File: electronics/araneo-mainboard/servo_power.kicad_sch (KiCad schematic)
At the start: 1 part

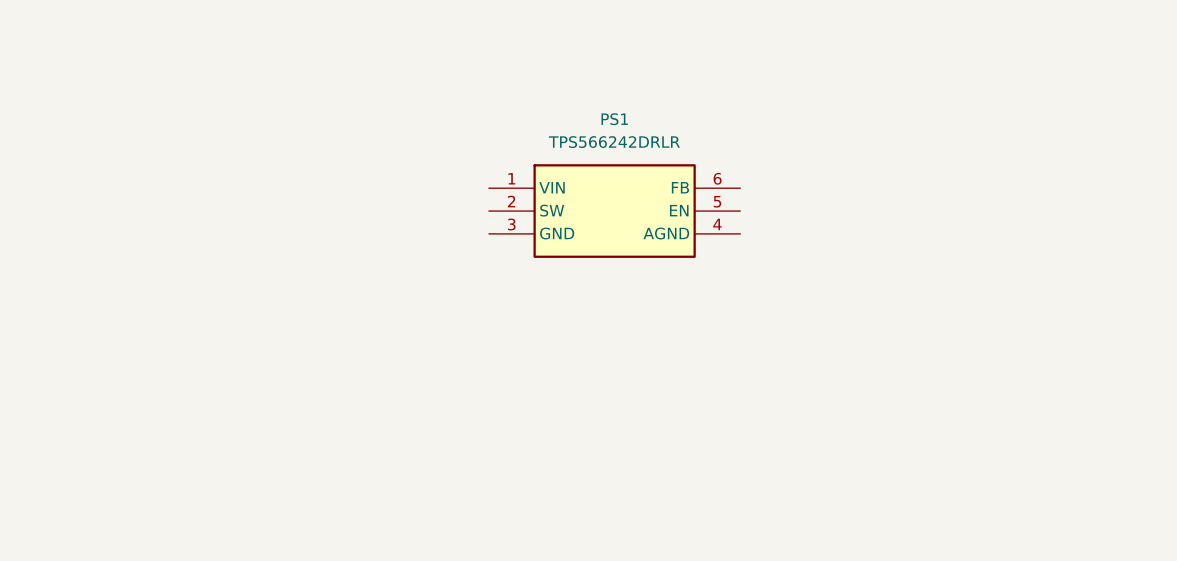
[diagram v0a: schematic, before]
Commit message: add components schematics
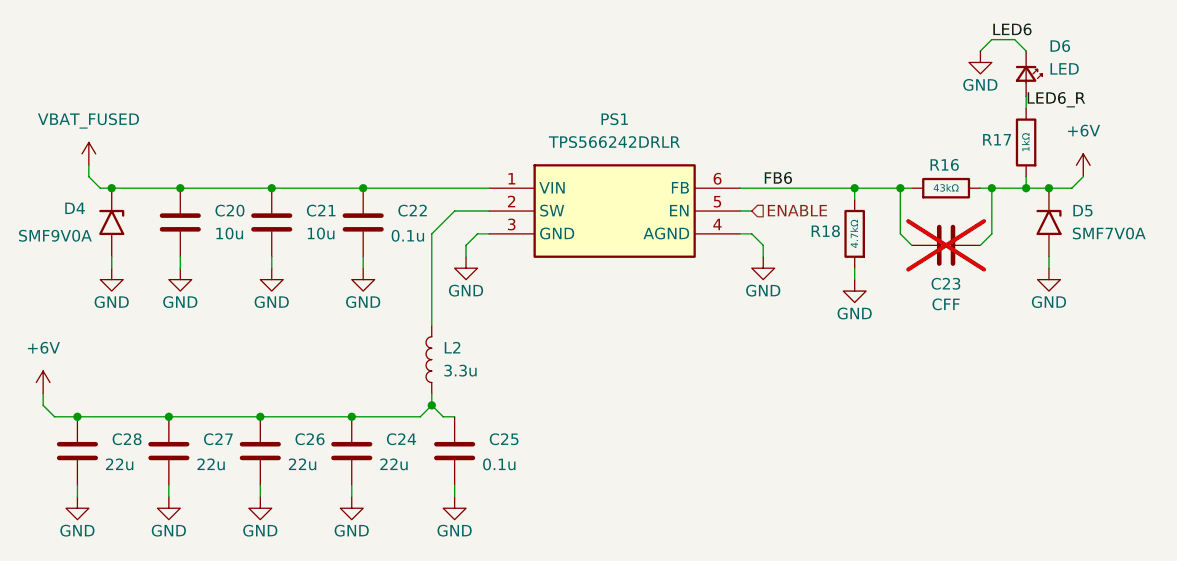
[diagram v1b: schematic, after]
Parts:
- added C20, C21: 10u, Diode_SMD:D_SMF, symbol Device:C
- added C22, C25: 0.1u, Diode_SMD:D_SMF, symbol Device:C
- added C23: CFF, Diode_SMD:D_SMF, symbol Device:C
- added C24, C26, C27, C28: 22u, Diode_SMD:D_SMF, symbol Device:C
- added D4: SMF9V0A, Diode_SMD:D_SMF, symbol Diode:SMF9V0A
- added D5: SMF7V0A, Diode_SMD:D_SMF, symbol Diode:SMF7V0A
- added D6: LED, PCM_SparkFun-LED:LED_0603_1608Metric, symbol PCM_SparkFun-LED:LED
- added L2: 3.3u, PCM_SparkFun-LED:LED_0603_1608Metric, symbol Device:L
- added R16: 43kΩ, PCM_JLCPCB:R_0402, symbol PCM_JLCPCB-Resistors:0402,1.2kΩ
- added R17: 1kΩ, PCM_JLCPCB:R_0402, symbol PCM_JLCPCB-Resistors:0402,1.2kΩ
- added R18: 4.7kΩ, PCM_JLCPCB:R_0402, symbol PCM_JLCPCB-Resistors:0402,1.2kΩ
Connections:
- net VBAT_FUSED: now reaches PS1.1 (VIN)
- net VBAT_FUSED: now also C20.1, C21.1, C22.1, D4.1 (A1)
- net at PS1.2 (SW): now also L2.2
- net GND: now reaches PS1.3 (GND)
- net GND: now also PS1.4 (AGND), C20.2, C21.2, C22.2, C24.2, C25.2, C26.2, C27.2, C28.2, D4.2 (A2), D5.2 (A2), D6.1 (K), R18.1
- net ENABLE: now reaches PS1.5 (EN)
- net FB6: now reaches PS1.6 (FB)
- net FB6: now also C23.1, R16.1, R18.2
- new net +6V: C23.2, C24.1, C25.1, C26.1, C27.1, C28.1, D5.1 (A1), L2.1, R16.2, R17.1
- new net LED6_R: D6.2 (A), R17.2

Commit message: electronics: assign footprints
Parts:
- C20, C21, C23: footprint Diode_SMD:D_SMF -> PCM_JLCPCB:C_0603
- C22, C25: footprint Diode_SMD:D_SMF -> PCM_JLCPCB:C_0402
- C24, C26, C27, C28: footprint Diode_SMD:D_SMF -> PCM_JLCPCB:C_0805
- D5: footprint Diode_SMD:D_SMF -> Diode_SMD:D_SOD-123
- D6: footprint PCM_SparkFun-LED:LED_0603_1608Metric -> PCM_JLCPCB:D_0603
- L2: footprint PCM_SparkFun-LED:LED_0603_1608Metric -> Custom:INDPM112100X400N
- PS1: footprint SOT50P160X60-6N -> Custom:SOT50P160X60-6N
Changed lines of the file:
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@@
 			)
 		)
-		(property "Footprint" "Diode_SMD:D_SMF"
+		(property "Footprint" "PCM_JLCPCB:C_0402"
 			(at 103.8352 69.85 0)
 			(hide yes)
@@
 			)
 		)
-		(property "Footprint" "Diode_SMD:D_SMF"
+		(property "Footprint" "PCM_JLCPCB:C_0805"
 			(at 72.0852 95.25 0)
 			(hide yes)
@@
 			)
 		)
-		(property "Footprint" "Diode_SMD:D_SMF"
+		(property "Footprint" "PCM_JLCPCB:C_0603"
 			(at 171.45 67.6148 0)
 			(hide yes)
@@
 			)
 		)
-		(property "Footprint" "Diode_SMD:D_SMF"
+		(property "Footprint" "PCM_JLCPCB:C_0402"
 			(at 113.9952 95.25 0)
 			(hide yes)
@@
 			)
 		)
-		(property "Footprint" "Diode_SMD:D_SMF"
+		(property "Footprint" "PCM_JLCPCB:C_0805"
 			(at 102.5652 95.25 0)
 			(hide yes)
@@
 			)
 		)
-		(property "Footprint" "PCM_SparkFun-LED:LED_0603_1608Metric"
+		(property "Footprint" "Custom:INDPM112100X400N"
 			(at 110.49 81.28 0)
 			(hide yes)
@@
 			)
 		)
-		(property "Footprint" "Diode_SMD:D_SMF"
+		(property "Footprint" "PCM_JLCPCB:C_0603"
 			(at 93.6752 69.85 0)
 			(hide yes)
@@
 			)
 		)
-		(property "Footprint" "Diode_SMD:D_SMF"
+		(property "Footprint" "PCM_JLCPCB:C_0805"
 			(at 82.2452 95.25 0)
 			(hide yes)
@@
 			)
 		)
-		(property "Footprint" "SOT50P160X60-6N"
+		(property "Footprint" "Custom:SOT50P160X60-6N"
 			(at 140.97 157.15 0)
 			(hide yes)
@@
 			)
 		)
-		(property "Footprint" "Diode_SMD:D_SMF"
+		(property "Footprint" "Diode_SMD:D_SOD-123"
 			(at 173.99 66.04 0)
 			(hide yes)
@@
 			)
 		)
-		(property "Footprint" "PCM_SparkFun-LED:LED_0603_1608Metric"
+		(property "Footprint" "PCM_JLCPCB:D_0603"
 			(at 171.45 49.53 0)
 			(hide yes)
@@
 			)
 		)
-		(property "Footprint" "Diode_SMD:D_SMF"
+		(property "Footprint" "PCM_JLCPCB:C_0805"
 			(at 92.4052 95.25 0)
 			(hide yes)
@@
 			)
 		)
-		(property "Footprint" "Diode_SMD:D_SMF"
+		(property "Footprint" "PCM_JLCPCB:C_0603"
 			(at 83.5152 69.85 0)
 			(hide yes)

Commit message: add first layout
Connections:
- net SW: now reaches L2.2, PS1.2 (SW)
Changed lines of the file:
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@@
+		)
+	)
+	(label "SW"
+		(at 110.49 74.93 90)
+		(effects
+			(font
+				(size 1.27 1.27)
+			)
+			(justify left bottom)
 		)
 	)

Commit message: electronics: update bom
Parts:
- D6, L2: now left out of the parts list
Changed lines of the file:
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@@
 		(body_style 1)
 		(exclude_from_sim no)
-		(in_bom yes)
+		(in_bom no)
 		(on_board yes)
 		(in_pos_files yes)
@@
 		(body_style 1)
 		(exclude_from_sim no)
-		(in_bom yes)
-		(on_board yes)
-		(in_pos_files yes)
+		(in_bom no)
+		(on_board yes)
+		(in_pos_files yes)

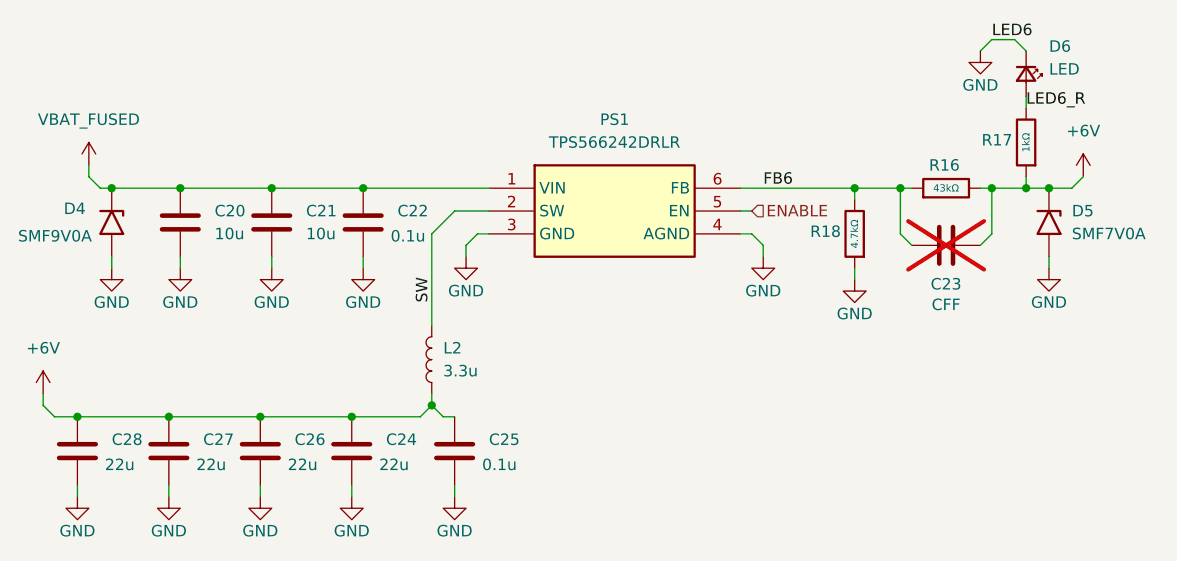
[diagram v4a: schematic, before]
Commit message: improve schematic and layout, add LCSC parts
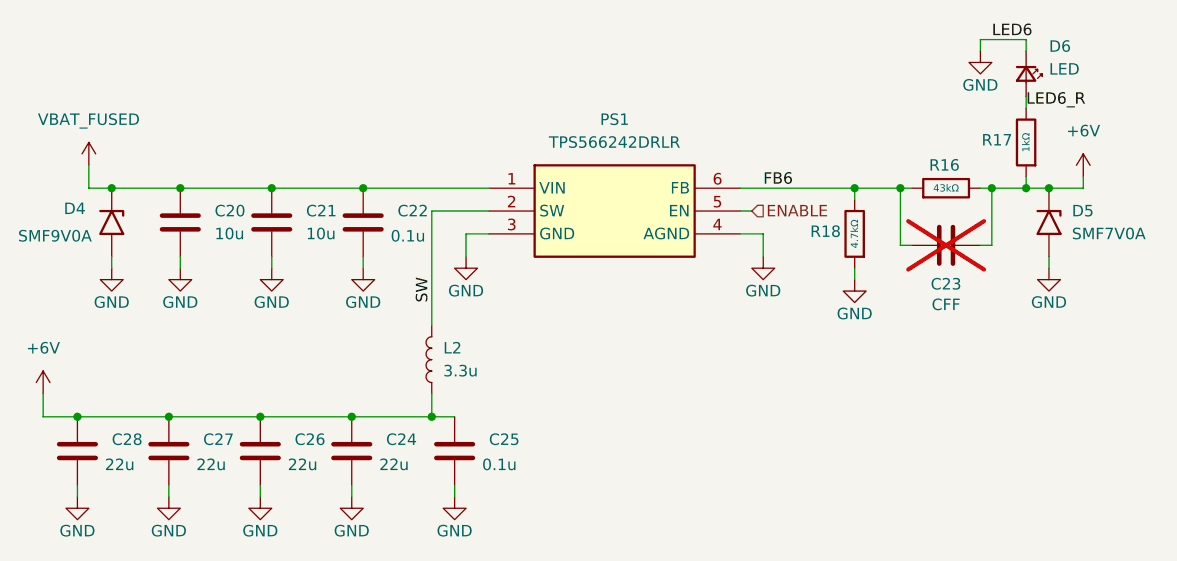
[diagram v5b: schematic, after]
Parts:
- D4, D5: now left out of the parts list
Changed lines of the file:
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@@
 	)
 	(junction
-		(at 110.49 86.36)
-		(diameter 0)
-		(color 0 0 0 0)
-	)
-	(junction
 		(at 82.55 62.23)
 		(diameter 0)
@@
 	)
 	(junction
+		(at 110.49 87.63)
+		(diameter 0)
+		(color 0 0 0 0)
+	)
+	(junction
 		(at 91.44 87.63)
 		(diameter 0)
@@
 	(wire
 		(pts
-			(xy 172.72 62.23) (xy 176.53 62.23)
+			(xy 171.45 45.72) (xy 171.45 46.99)
 		)
 		(stroke
@@
 	(wire
 		(pts
-			(xy 81.28 95.25) (xy 81.28 96.52)
+			(xy 172.72 62.23) (xy 176.53 62.23)
 		)
 		(stroke
@@
 	(wire
 		(pts
-			(xy 113.03 64.77) (xy 110.49 67.31)
+			(xy 81.28 95.25) (xy 81.28 96.52)
 		)
 		(stroke
@@
 	(wire
 		(pts
-			(xy 179.07 69.85) (xy 179.07 71.12)
+			(xy 72.39 59.69) (xy 72.39 62.23)
 		)
 		(stroke
@@
 	(wire
 		(pts
-			(xy 147.32 68.58) (xy 147.32 69.85)
+			(xy 67.31 87.63) (xy 71.12 87.63)
 		)
 		(stroke
@@
 	(wire
 		(pts
-			(xy 113.03 64.77) (xy 116.84 64.77)
+			(xy 179.07 69.85) (xy 179.07 71.12)
 		)
 		(stroke
@@
 	(wire
 		(pts
-			(xy 171.45 68.58) (xy 172.72 67.31)
+			(xy 72.39 62.23) (xy 74.93 62.23)
 		)
 		(stroke
@@
 	(wire
 		(pts
-			(xy 101.6 95.25) (xy 101.6 96.52)
+			(xy 162.56 62.23) (xy 162.56 68.58)
 		)
 		(stroke
@@
 	(wire
 		(pts
-			(xy 113.03 95.25) (xy 113.03 96.52)
+			(xy 101.6 95.25) (xy 101.6 96.52)
 		)
 		(stroke
@@
 	(wire
 		(pts
-			(xy 176.53 52.07) (xy 176.53 53.34)
+			(xy 113.03 95.25) (xy 113.03 96.52)
 		)
 		(stroke
@@
 	(wire
 		(pts
-			(xy 91.44 87.63) (xy 101.6 87.63)
+			(xy 176.53 52.07) (xy 176.53 53.34)
 		)
 		(stroke
@@
 	(wire
 		(pts
-			(xy 101.6 87.63) (xy 109.22 87.63)
+			(xy 91.44 87.63) (xy 101.6 87.63)
 		)
 		(stroke
@@
 	(wire
 		(pts
-			(xy 171.45 46.99) (xy 172.72 45.72)
+			(xy 101.6 87.63) (xy 110.49 87.63)
 		)
 		(stroke
@@
 	(wire
 		(pts
-			(xy 144.78 67.31) (xy 146.05 67.31)
+			(xy 144.78 67.31) (xy 147.32 67.31)
 		)
 		(stroke
@@
 	(wire
 		(pts
-			(xy 157.48 71.12) (xy 157.48 72.39)
+			(xy 171.45 45.72) (xy 176.53 45.72)
 		)
 		(stroke
@@
 	(wire
 		(pts
-			(xy 68.58 87.63) (xy 71.12 87.63)
+			(xy 157.48 71.12) (xy 157.48 72.39)
 		)
 		(stroke
@@
 	(wire
 		(pts
-			(xy 73.66 62.23) (xy 74.93 62.23)
-		)
-		(stroke
-			(width 0)
-			(type default)
-		)
-	)
-	(wire
-		(pts
-			(xy 110.49 67.31) (xy 110.49 77.47)
-		)
-		(stroke
-			(width 0)
-			(type default)
-		)
-	)
-	(wire
-		(pts
-			(xy 72.39 59.69) (xy 72.39 60.96)
+			(xy 110.49 64.77) (xy 110.49 77.47)
 		)
 		(stroke
@@
 	(wire
 		(pts
-			(xy 110.49 85.09) (xy 110.49 86.36)
+			(xy 110.49 85.09) (xy 110.49 87.63)
 		)
 		(stroke
@@
 	(wire
 		(pts
-			(xy 115.57 67.31) (xy 116.84 67.31)
+			(xy 114.3 67.31) (xy 116.84 67.31)
 		)
 		(stroke
@@
 	(wire
 		(pts
-			(xy 72.39 60.96) (xy 73.66 62.23)
+			(xy 110.49 87.63) (xy 113.03 87.63)
 		)
 		(stroke
@@
 	(wire
 		(pts
-			(xy 109.22 87.63) (xy 110.49 86.36)
-		)
-		(stroke
-			(width 0)
-			(type default)
-		)
-	)
-	(wire
-		(pts
 			(xy 157.48 62.23) (xy 157.48 63.5)
 		)
@@
 	(wire
 		(pts
-			(xy 172.72 45.72) (xy 175.26 45.72)
-		)
-		(stroke
-			(width 0)
-			(type default)
-		)
-	)
-	(wire
-		(pts
 			(xy 74.93 69.85) (xy 74.93 71.12)
 		)
@@
 	(wire
 		(pts
-			(xy 179.07 62.23) (xy 181.61 62.23)
+			(xy 179.07 62.23) (xy 182.88 62.23)
 		)
 		(stroke
@@
 	(wire
 		(pts
-			(xy 110.49 86.36) (xy 111.76 87.63)
-		)
-		(stroke
-			(width 0)
-			(type default)
-		)
-	)
-	(wire
-		(pts
-			(xy 182.88 60.96) (xy 181.61 62.23)
+			(xy 182.88 60.96) (xy 182.88 62.23)
 		)
 		(stroke
@@
 	(wire
 		(pts
-			(xy 175.26 45.72) (xy 176.53 46.99)
+			(xy 162.56 68.58) (xy 163.83 68.58)
 		)
 		(stroke
@@
 	(wire
 		(pts
-			(xy 172.72 62.23) (xy 172.72 67.31)
+			(xy 172.72 62.23) (xy 172.72 68.58)
 		)
 		(stroke
@@
 	(wire
 		(pts
-			(xy 144.78 64.77) (xy 146.05 64.77)
+			(xy 171.45 68.58) (xy 172.72 68.58)
 		)
 		(stroke
@@
 	(wire
 		(pts
-			(xy 162.56 62.23) (xy 162.56 67.31)
-		)
-		(stroke
-			(width 0)
-			(type default)
-		)
-	)
-	(wire
-		(pts
-			(xy 114.3 68.58) (xy 115.57 67.31)
+			(xy 144.78 64.77) (xy 146.05 64.77)
 		)
 		(stroke
@@
 	(wire
 		(pts
-			(xy 111.76 87.63) (xy 113.03 87.63)
+			(xy 176.53 45.72) (xy 176.53 46.99)
 		)
 		(stroke
@@
 	(wire
 		(pts
-			(xy 67.31 86.36) (xy 68.58 87.63)
-		)
-		(stroke
-			(width 0)
-			(type default)
-		)
-	)
-	(wire
-		(pts
-			(xy 114.3 68.58) (xy 114.3 69.85)
+			(xy 114.3 67.31) (xy 114.3 69.85)
 		)
 		(stroke
@@
 	(wire
 		(pts
-			(xy 147.32 68.58) (xy 146.05 67.31)
+			(xy 110.49 64.77) (xy 116.84 64.77)
 		)
 		(stroke
@@
 	(wire
 		(pts
-			(xy 67.31 85.09) (xy 67.31 86.36)
+			(xy 67.31 85.09) (xy 67.31 87.63)
 		)
 		(stroke
@@
 	(wire
 		(pts
-			(xy 163.83 68.58) (xy 162.56 67.31)
+			(xy 147.32 67.31) (xy 147.32 69.85)
 		)
 		(stroke
@@
 		(body_style 1)
 		(exclude_from_sim no)
-		(in_bom yes)
+		(in_bom no)
 		(on_board yes)
 		(in_pos_files yes)
@@
 		(body_style 1)
 		(exclude_from_sim no)
-		(in_bom yes)
+		(in_bom no)
 		(on_board yes)
 		(in_pos_files yes)
